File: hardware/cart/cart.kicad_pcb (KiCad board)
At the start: 2 copper layers, 40.1 x 29.7 mm, 6 parts, among them J1 Front Edge, J2 Back Edge, U1 Pro Micro

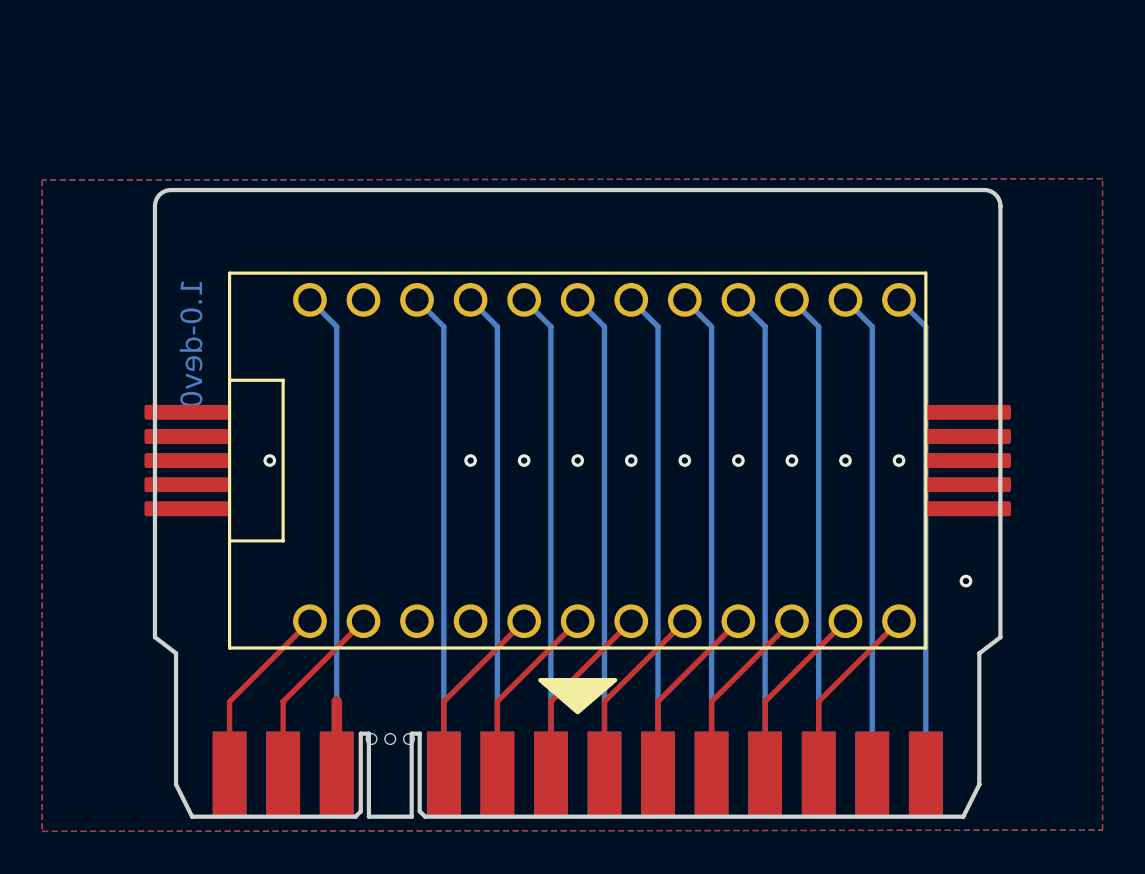
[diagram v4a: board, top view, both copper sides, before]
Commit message: Add grip slot to cart
- Extends cart by 0.24 in
- Update to 1.0-dev1
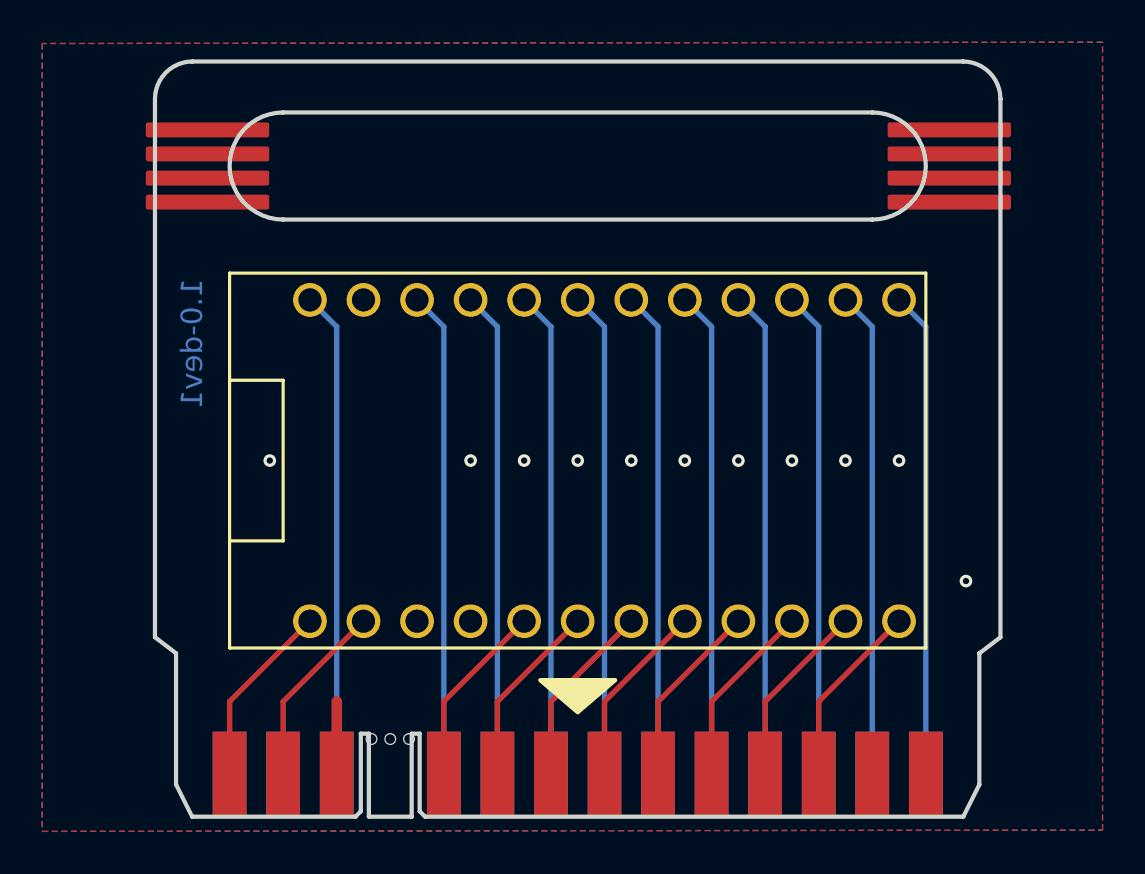
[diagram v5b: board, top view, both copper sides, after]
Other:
- board size 40.1 x 29.7 mm -> 40.1 x 35.8 mm
- board text added: "1.0-dev1"
- board text removed: "1.0-dev0"
